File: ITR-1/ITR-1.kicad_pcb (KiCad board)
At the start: 2 copper layers, 30 x 40 mm, 4 parts, among them K1 кнопка

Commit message: схема организации питания
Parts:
- added C1: Конденсатор_керамический, N_RLC:Конденсатор_SMD_IEC_0805, F.Cu at (137.5, 47.5)
- added C2: Конденсатор_керамический, N_RLC:Конденсатор_SMD_IEC_0805, F.Cu at (137.5, 50.6)
- added C3: Конденсатор_керамический, N_RLC:Конденсатор_SMD_0603_pnp, F.Cu at (144.0, 47.4)
- added C4: Конденсатор_керамический, N_RLC:Конденсатор_SMD_IEC_0603, F.Cu at (141.8, 57.8)
- added C5: Конденсатор_керамический, N_RLC:Конденсатор_SMD_IEC_0603, F.Cu at (141.8, 60.5)
- added DD1: Микросхема_заряда_MCP73831T-2ACI_OT, N_G:SOT-23-5_pnp, F.Cu at (129.5, 31.8)
- added G2: ИОП_LM4040BIM3-2.5_NOPB, N_VD_HL:Транзистор_IRLML6344TR_SOT-23, F.Cu at (154.0, 40.0)
- added R1: Резистор_0,065Вт, N_RLC:Резистор_SMD_0603_0,065_Вт, F.Cu at (140.0, 35.7)
- added R10: Резистор_0,065Вт, N_RLC:Резистор_SMD_0603_0,065_Вт, F.Cu at (151.5, 64.2)
- added R11: Резистор_0,065Вт, N_RLC:Резистор_SMD_0603_0,065_Вт, F.Cu at (151.5, 67.3)
- added R12: Резистор_0,065Вт, N_RLC:Резистор_SMD_0603_0,065_Вт, F.Cu at (155.6, 64.2)
- added R2: Резистор_0,065Вт, N_RLC:Резистор_SMD_0603_0,065_Вт, F.Cu at (144.0, 35.7)
- added R3: Резистор_0,065Вт, N_RLC:Резистор_SMD_0603_0,065_Вт, F.Cu at (140.0, 38.8)
- added R4: Резистор_0,065Вт, N_RLC:Резистор_SMD_0603_0,065_Вт, F.Cu at (144.0, 38.8)
- added R5: Резистор_0,065Вт, N_RLC:Резистор_SMD_0603_0,065_Вт, F.Cu at (156.2, 49.2)
- added R6: Резистор_0,065Вт, N_RLC:Резистор_SMD_0603_0,065_Вт, F.Cu at (160.3, 49.2)
- added R7: Резистор_0,065Вт, N_RLC:Резистор_SMD_0603_0,065_Вт, F.Cu at (156.2, 52.3)
- added R8: Резистор_0,065Вт, N_RLC:Резистор_SMD_0603_0,065_Вт, F.Cu at (160.3, 52.3)
- added R9: Резистор_0,065Вт, N_RLC:Резистор_SMD_0603_0,065_Вт, F.Cu at (156.2, 55.4)
- added VD1: Диоды_шоттки_BAR43CFILM, N_VD_HL:Транзистор_IRLML6344TR_SOT-23, F.Cu at (152.0, 50.0)
- added VT1: Транзистор_полевой_P-канал(IRLML2246TRPBF), N_VD_HL:Транзистор_IRLML6344TR_SOT-23, F.Cu at (128.8, 38.2)
- added VT2: Транзистор_полевой_N-IRLML6344TR, N_VD_HL:Транзистор_IRLML6344TR_SOT-23, F.Cu at (135.8, 36.5)
- added VT3: Транзистор_полевой_N-IRLML6344TR, N_VD_HL:Транзистор_IRLML6344TR_SOT-23, F.Cu at (135.6, 41.0)
- added VT4: Транзистор_полевой_P-канал(IRLML2246TRPBF), N_VD_HL:Транзистор_IRLML6344TR_SOT-23, F.Cu at (152.0, 54.5)
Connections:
- G1 pad 1: (no net) -> /GND
- G1 pad 2: (no net) -> /3V3
- G1 pad 3: (no net) -> /BAT.LOAD
- G1 pad 4: (no net) -> /3V3

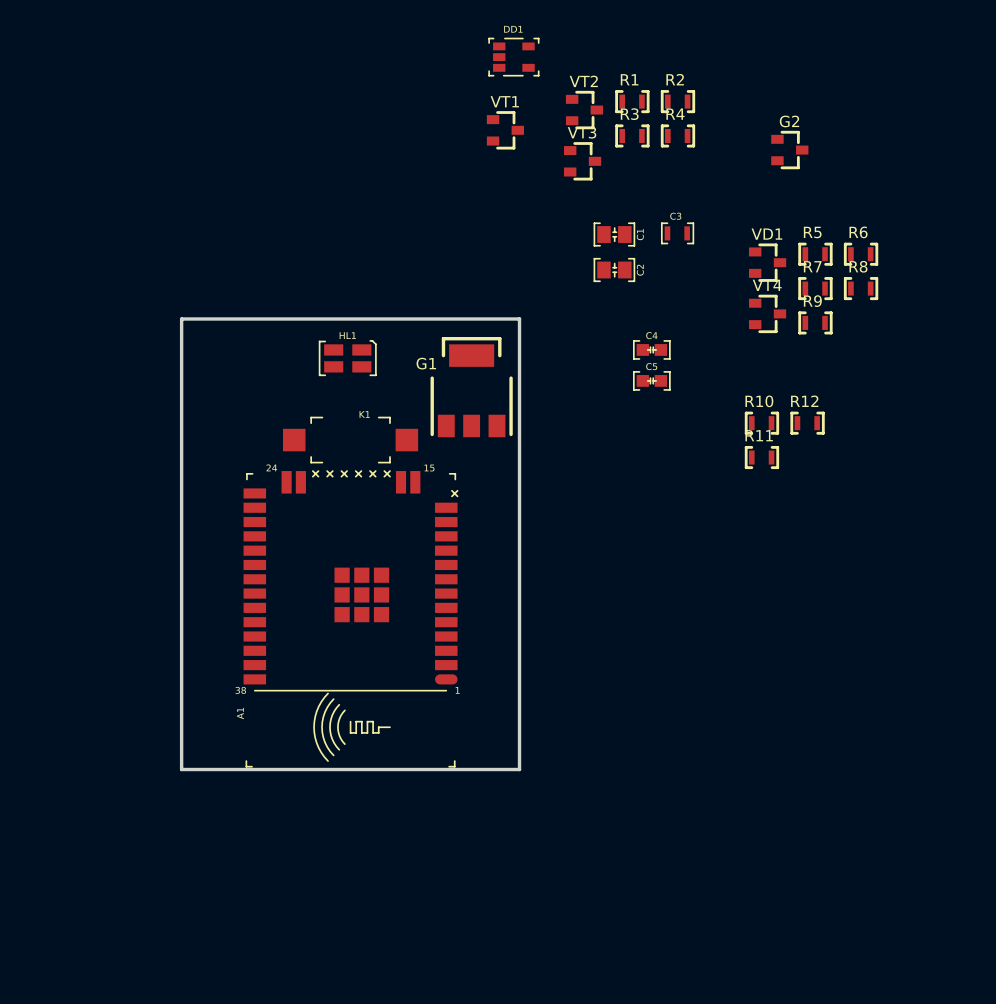
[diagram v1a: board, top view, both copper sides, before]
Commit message: закончена схема, начата трассировка питания
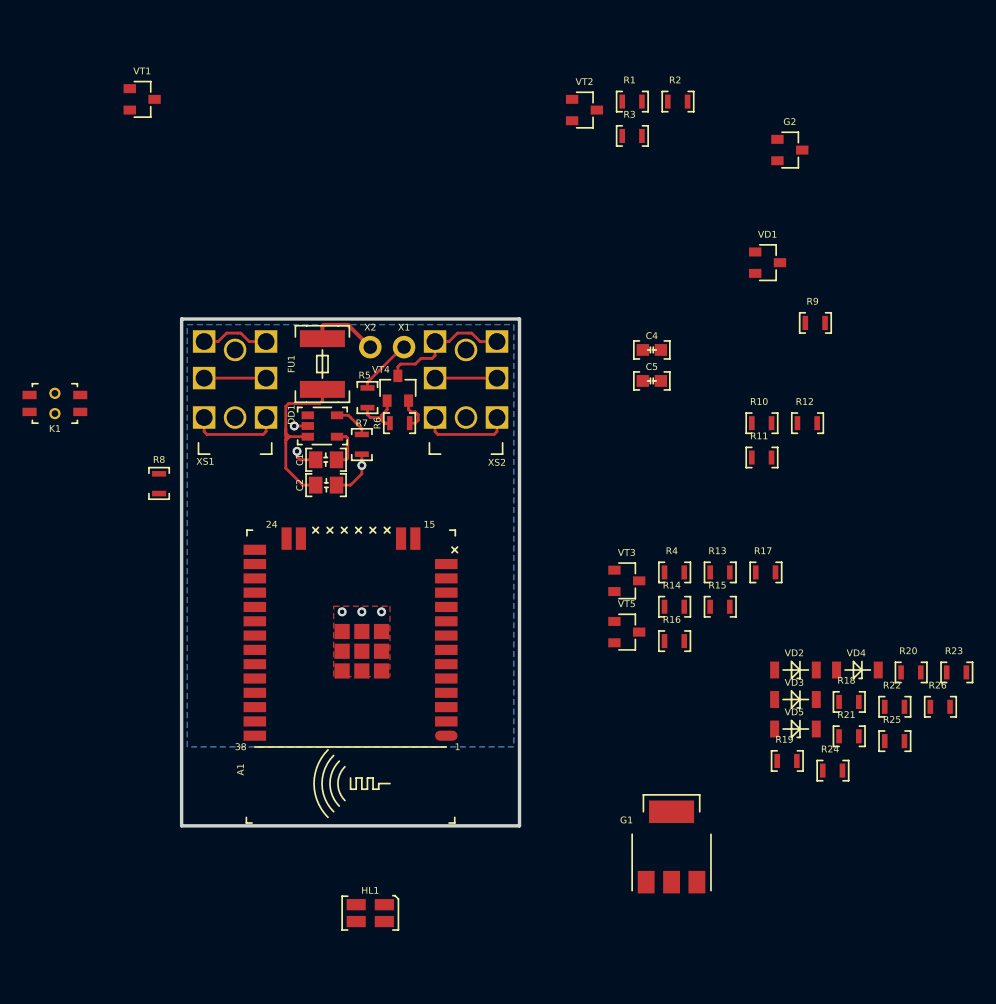
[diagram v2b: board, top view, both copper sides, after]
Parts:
- removed C3: Конденсатор_керамический, N_RLC:Конденсатор_SMD_0603_pnp
- added FU1: Предохранитель_MF-MSMF030, N_RLC:Предохранитель_SMD_1812, F.Cu at (112.5, 56.8)
- added R13: Резистор_0,065Вт, N_RLC:Резистор_SMD_0603_0,065_Вт, F.Cu at (147.8, 77.5)
- added R14: Резистор_0,065Вт, N_RLC:Резистор_SMD_0603_0,065_Вт, F.Cu at (143.8, 80.5)
- added R15: Резистор_0,065Вт, N_RLC:Резистор_SMD_0603_0,065_Вт, F.Cu at (147.8, 80.5)
- added R16: Резистор_0,065Вт, N_RLC:Резистор_SMD_0603_0,065_Вт, F.Cu at (143.8, 83.6)
- added R17: Резистор_0,065Вт, N_RLC:Резистор_SMD_0603_0,065_Вт, F.Cu at (151.8, 77.5)
- added R18: Резистор_0,065Вт, N_RLC:Резистор_SMD_0603_0,065_Вт, F.Cu at (159.2, 89.0)
- added R19: Резистор_0,065Вт, N_RLC:Резистор_SMD_0603_0,065_Вт, F.Cu at (153.8, 94.2)
- added R20: Резистор_0,065Вт, N_RLC:Резистор_SMD_0603_0,065_Вт, F.Cu at (164.8, 86.4)
- added R21: Резистор_0,065Вт, N_RLC:Резистор_SMD_0603_0,065_Вт, F.Cu at (159.2, 92.0)
- added R22: Резистор_0,065Вт, N_RLC:Резистор_SMD_0603_0,065_Вт, F.Cu at (163.3, 89.4)
- added R23: Резистор_0,065Вт, N_RLC:Резистор_SMD_0603_0,065_Вт, F.Cu at (168.8, 86.4)
- added R24: Резистор_0,065Вт, N_RLC:Резистор_SMD_0603_0,065_Вт, F.Cu at (157.8, 95.1)
- added R25: Резистор_0,065Вт, N_RLC:Резистор_SMD_0603_0,065_Вт, F.Cu at (163.3, 92.5)
- added R26: Резистор_0,065Вт, N_RLC:Резистор_SMD_0603_0,065_Вт, F.Cu at (167.3, 89.4)
- added VD2: Стабилитрон_BZV55C2V7, N_VD_HL:SOD-80, F.Cu at (152.6, 86.2)
- added VD3: Стабилитрон_BZV55C2V7, N_VD_HL:SOD-80, F.Cu at (152.6, 88.8)
- added VD4: Стабилитрон_BZV55C2V7, N_VD_HL:SOD-80, F.Cu at (158.1, 86.2)
- added VD5: Стабилитрон_BZV55-C3V9, N_VD_HL:SOD-80, F.Cu at (152.6, 91.4)
- added VT5: Транзистор_полевой_N-IRLML6344TR, N_VD_HL:Транзистор_IRLML6344TR_SOT-23, F.Cu at (139.5, 82.8)
- added X1: отверстие_под_пайку, N_X:ОтверстиеD1.2, F.Cu at (119.8, 57.5)
- added X2: отверстие_под_пайку, N_X:ОтверстиеD1.2, F.Cu at (116.8, 57.5)
- added XS1: Клеммник_х3, N_X:jack_ST-033, F.Cu at (102.2, 63.8)
- added XS2: Клеммник_х3, N_X:jack_ST-033, F.Cu at (122.8, 63.8)
- K1: value кнопка -> Кнопка_KLS7-TS5401-1.35-250-T; footprint N_X:Кнопка_FSMSM -> N_X:Кнопка_KLS7-TS5401
- moved R8 64.7 mm to (98.0, 69.6), turned to 90 degrees
- moved HL1 49.3 mm to (118.0, 107.0)
- moved G1 44.2 mm to (143.5, 101.2)
- moved R6 43.6 mm to (119.4, 64.2), turned to 180 degrees
- moved R7 42.6 mm to (116.0, 66.1), turned to 270 degrees
- moved R5 41.7 mm to (116.5, 62.0), turned to 90 degrees
- moved R4 38.8 mm to (143.8, 77.5)
- moved VT3 37.5 mm to (139.5, 78.2)
- moved DD1 36.9 mm to (112.5, 64.5)
- moved VT4 33.5 mm to (119.2, 61.1), turned to 90 degrees
- moved VT1 32.4 mm to (96.5, 35.5)
- moved C2 31.9 mm to (111.9, 69.8)
- moved C1 31.0 mm to (113.8, 67.5), turned to 180 degrees
- moved K1 19.4 mm to (91.0, 61.8), turned to 180 degrees
- moved A1 5.00 mm to (115.0, 83.0)
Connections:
- net /BAT.IN renamed Net-(C2-Pad1)
- net Net-(R9-Pad2) renamed /EXT.BUTT
- A1 pad 1: (no net) -> /GND
- A1 pad 11: (no net) -> /BUTT.TURN
- A1 pad 13: (no net) -> /CHARGE.MODE
- A1 pad 15: (no net) -> /GND
- A1 pad 2: (no net) -> /3V3
- A1 pad 25: (no net) -> /BOOT
- A1 pad 29: (no net) -> /LED.RED
- A1 pad 3: (no net) -> /RESET
- A1 pad 31: (no net) -> /LED.GREEN
- A1 pad 34: (no net) -> /UART.RX
- A1 pad 35: (no net) -> /UART.TX
- A1 pad 38: (no net) -> /GND
- A1 pad 39: Net-(A1-Pad39) -> /GND
- A1 pad 6: (no net) -> /2V5.REF
- A1 pad 7: (no net) -> /BAT.MEASURE
- A1 pad 9: (no net) -> /SELF.TURN
- HL1 pad 1: (no net) -> /3V3
- HL1 pad 2: (no net) -> Net-(HL1-Pad2)
- HL1 pad 3: (no net) -> /3V3
- HL1 pad 4: (no net) -> Net-(HL1-Pad4)
- K1 pad 1: (no net) -> Net-(K1-Pad1)
- K1 pad 2: (no net) -> Net-(K1-Pad1)
- R3 pad 1: (no net) -> /SELF.TURN
- R4 pad 1: (no net) -> Net-(R14-Pad2)
- R4 pad 2: (no net) -> /LED.GREEN
- R8 pad 1: (no net) -> /CHARGE.MODE
- R9 pad 1: (no net) -> /BUTT.TURN
- VT3 pad 1: (no net) -> Net-(R14-Pad2)
- VT3 pad 2: (no net) -> /GND
- VT3 pad 3: (no net) -> Net-(R16-Pad2)
- VT4 pad 3: (no net) -> /U.IN
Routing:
- net /GND: track 0.00 -> 21.1 mm, vias 0 -> 6
- net Net-(C2-Pad1): track 0.00 -> 16.7 mm
- net /U.IN: track 0.00 -> 11.9 mm
- net /OUT.BOOT: track 0.00 -> 8.21 mm
- net /U.PROTECT: track 0.00 -> 7.01 mm
- net /BAT.IN: track 0.00 -> 6.22 mm
- net /OUT.RX: track 0.00 -> 6.12 mm
- net /OUT.TX: track 0.00 -> 5.50 mm
- net /EXT.BUTT: track 0.00 -> 5.50 mm
- net Net-(R5-Pad1): track 0.00 -> 5.04 mm
- net Net-(DD1-Pad5): track 0.00 -> 3.20 mm
- added copper zone on B.Cu, net /GND
- added copper zone on F.Cu, net /GND
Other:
- board size 30 x 40 mm -> 30 x 45 mm
- net class BATT added: clearance 0.2, trace_width 0.35, via_dia 1, via_drill 0.6

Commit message: подготовлена трассировка питания, упрощена схема подключения периферии
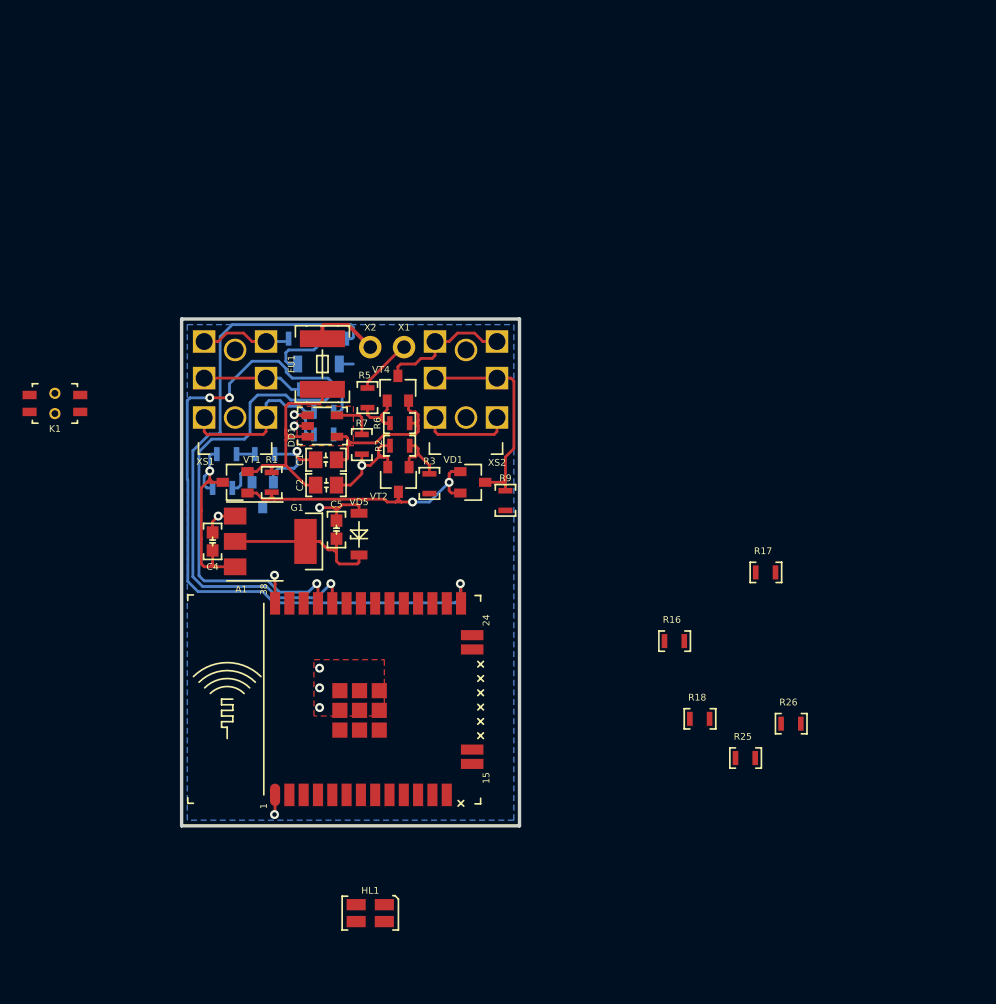
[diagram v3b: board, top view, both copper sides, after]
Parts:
- removed R13, R14, R15, R23, R24, R4: Резистор_0,065Вт, N_RLC:Резистор_SMD_0603_0,065_Вт
- removed VD2, VD3: Стабилитрон_BZV55C2V7, N_VD_HL:SOD-80
- removed VT3, VT5: Транзистор_полевой_N-IRLML6344TR, N_VD_HL:Транзистор_IRLML6344TR_SOT-23
- G2, R10, R11, R12, R19, R20, R21, R22, R8, VD4: moved to B.Cu
- moved R22 59.4 mm to (113.8, 56.8), turned to 180 degrees
- moved R20 59.0 mm to (111.4, 61.2), turned to 180 degrees
- moved R19 57.3 mm to (110.4, 56.8), turned to 180 degrees
- moved G2 55.9 mm to (107.2, 70.6), turned to 270 degrees
- moved R21 54.8 mm to (112.6, 63.2), turned to 180 degrees
- moved R12 52.2 mm to (103.6, 70.0)
- moved VD4 51.8 mm to (114.0, 59.0), turned to 180 degrees
- moved R10 47.6 mm to (104.0, 67.0)
- moved R1 46.5 mm to (108.0, 69.5), turned to 270 degrees
- moved R11 44.1 mm to (107.4, 67.0)
- moved G1 43.9 mm to (108.5, 74.8), turned to 270 degrees
- moved C4 42.5 mm to (102.8, 74.8), turned to 90 degrees
- moved VD5 41.6 mm to (115.8, 72.2), turned to 270 degrees
- moved R2 39.3 mm to (119.4, 66.2), turned to 180 degrees
- moved VT2 36.7 mm to (119.2, 69.2), turned to 270 degrees
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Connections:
- net Net-(C2-Pad1) renamed /BAT.CHARGE
- A1 pad 29: /LED.RED -> /LED.GREEN
- A1 pad 31: /LED.GREEN -> /LED.RED
- HL1 pad 1: /3V3 -> Net-(HL1-Pad1)
- HL1 pad 2: Net-(HL1-Pad2) -> /GND
- HL1 pad 3: /3V3 -> Net-(HL1-Pad3)
- HL1 pad 4: Net-(HL1-Pad4) -> /GND
- R16 pad 1: Net-(HL1-Pad4) -> Net-(HL1-Pad1)
- R16 pad 2: Net-(R16-Pad2) -> /LED.RED
- R17 pad 1: Net-(HL1-Pad2) -> Net-(HL1-Pad3)
- R17 pad 2: Net-(R17-Pad2) -> /LED.GREEN
- R18 pad 1: Net-(R18-Pad1) -> /BOOT
- R20 pad 1: Net-(R20-Pad1) -> /UART.TX
- R21 pad 1: Net-(R18-Pad1) -> /BOOT
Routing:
- net /BOOT: track 0.00 -> 63.6 mm, vias 0 -> 3
- net /UART.RX: track 0.00 -> 52.1 mm, vias 0 -> 1
- net /UART.TX: track 0.00 -> 40.9 mm, vias 0 -> 1
- net /GND: track 21.1 -> 48.6 mm, vias 6 -> 10
- net Net-(R1-Pad2): track 0.00 -> 25.0 mm, vias 0 -> 2
- net /BAT.LOAD: track 0.00 -> 19.7 mm, vias 0 -> 1
- net /3V3: track 0.00 -> 14.6 mm
- net /EXT.BUTT: track 5.50 -> 19.4 mm
- net /U.PROTECT: track 7.01 -> 15.7 mm
- net Net-(R19-Pad1): track 0.00 -> 7.69 mm
- net /OUT.BOOT: track 8.21 -> 14.2 mm
- net Net-(R2-Pad1): track 0.00 -> 5.26 mm
- net /BAT.CHARGE: track 16.7 -> 21.2 mm
- net Net-(DD1-Pad1): track 0.00 -> 4.32 mm, vias 0 -> 1
- net /2V5.REF: track 0.00 -> 3.84 mm
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- added copper zone on F.Cu, net /BAT.CHARGE

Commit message: обновлены посадочные места и схема питания
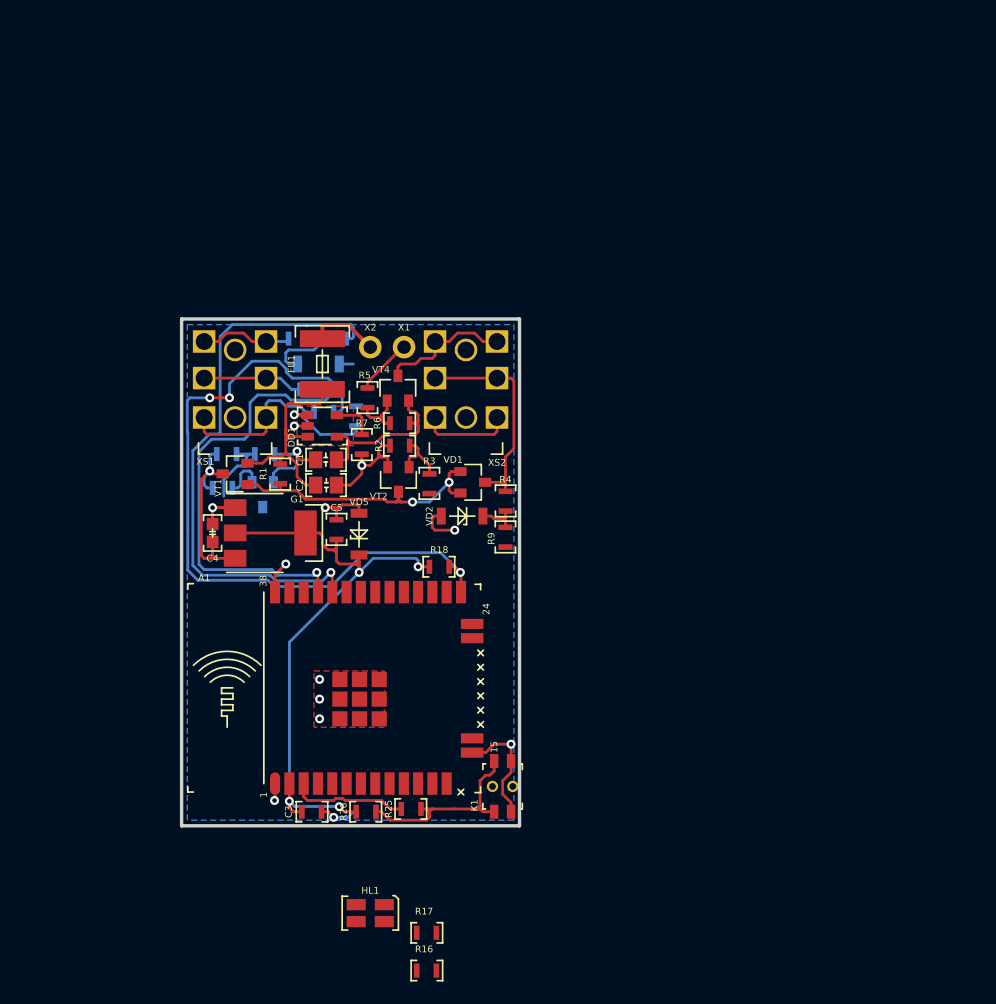
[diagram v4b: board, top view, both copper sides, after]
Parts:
- added C3: Конденсатор_керамический, N_RLC:Конденсатор_SMD_0603_pnp, F.Cu at (111.5, 98.8)
- added R4: Резистор_0,065Вт, N_RLC:Резистор_SMD_0603_0,065_Вт, F.Cu at (128.8, 71.2)
- added VD2: Стабилитрон_BZV55-C3V9, N_VD_HL:SOD-80, F.Cu at (123.0, 72.5)
- C5: footprint N_RLC:Конденсатор_SMD_IEC_0603 -> N_RLC:Конденсатор_SMD_0603_pnp
- moved K1 53.2 mm to (129.2, 98.8), turned to 90 degrees
- moved R17 43.9 mm to (121.8, 109.5)
- moved R26 38.5 mm to (116.4, 98.8), turned to 180 degrees
- moved R16 36.6 mm to (121.8, 112.8)
- moved R25 30.0 mm to (120.4, 98.5), turned to 180 degrees
- moved R18 26.8 mm to (122.9, 77.0), turned to 180 degrees
- moved R8 3.30 mm to (115.5, 63.6), turned to 270 degrees
- moved R9 3.25 mm to (128.8, 74.4)
- moved R1 1.06 mm to (108.8, 68.8)
- moved A1 1.00 mm to (117.3, 87.8)
- moved C4 0.75 mm to (102.8, 74.0)
- moved G1 0.75 mm to (108.5, 74.0)
- moved VT1 0.75 mm to (104.8, 68.8)
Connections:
- net /BAT.MEASURE renamed /AN.BAT.MEASURE
- A1 pad 5: (no net) -> /AN.2V5.REF
- A1 pad 6: /2V5.REF -> (no net)
- G2 pad 1: /2V5.REF -> /AN.2V5.REF
- R12 pad 2: /2V5.REF -> /AN.2V5.REF
- R9 pad 2: /EXT.BUTT -> Net-(R4-Pad1)
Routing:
- net /3V3: track 14.6 -> 57.4 mm, vias 0 -> 4
- net /GND: track 48.6 -> 68.8 mm, vias 10 -> 13
- net Net-(K1-Pad1): track 0.00 -> 18.6 mm
- net /RESET: track 0.00 -> 10.4 mm
- net /AN.BAT.MEASURE: track 1.62 -> 7.35 mm
- net Net-(R4-Pad1): track 0.00 -> 4.06 mm
- net /AN.2V5.REF: track 0.00 -> 3.84 mm
- net /2V5.REF: track 3.84 -> 0.00 mm
- net Net-(DD1-Pad1): track 4.32 -> 8.05 mm
- net /UART.TX: track 40.9 -> 39.5 mm
- net /UART.RX: track 52.1 -> 50.6 mm
- net /BAT.LOAD: track 19.7 -> 18.4 mm
- net Net-(R1-Pad2): track 25.0 -> 25.8 mm
- net /BOOT: track 63.6 -> 64.2 mm

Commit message: подготовлена трассировка +PNG +STP, требуется контрольная проверка
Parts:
- removed R16: Резистор_0,065Вт, N_RLC:Резистор_SMD_0603_0,065_Вт
- added D1: LOGO, N_ICO:ni_10x10, B.Cu at (105.0, 89.0)
- added D2: LOGO, N_ICO:VLAD_10x10, B.Cu at (116.0, 88.8)
- HL1: value Светодиод_сдвоенный_KPB-3025SURKCGKC -> Светодиод; footprint N_VD_HL:Светодиод_SMD_m3025 -> N_VD_HL:Светодиод_SMD_IEC_0603
- moved R17 35.0 mm to (120.5, 74.5), turned to 270 degrees
- moved HL1 32.3 mm to (118.5, 74.8), turned to 90 degrees
- moved R18 3.88 mm to (126.8, 77.0), turned to 0 degrees
- moved R9 2.00 mm to (126.8, 74.5), turned to 0 degrees
- moved C4 0.67 mm to (103.2, 74.5)
- moved C5 0.50 mm to (114.2, 73.7)
- moved G1 0.50 mm to (109.0, 74.0)
- moved VD5 0.50 mm to (116.2, 72.2)
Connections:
- A1 pad 11: /BUTT.TURN -> (no net)
- A1 pad 13: /CHARGE.MODE -> (no net)
- A1 pad 24: (no net) -> /AN.2V5.REF
- A1 pad 26: (no net) -> /AN.BAT.MEASURE
- A1 pad 28: (no net) -> /BUTT.TURN
- A1 pad 29: /LED.GREEN -> /SELF.TURN
- A1 pad 30: (no net) -> /LED
- A1 pad 31: /LED.RED -> /CHARGE.MODE
- A1 pad 5: /AN.2V5.REF -> (no net)
- A1 pad 7: /AN.BAT.MEASURE -> (no net)
- A1 pad 9: /SELF.TURN -> (no net)
- R17 pad 1: Net-(HL1-Pad3) -> Net-(HL1-PadA)
- R17 pad 2: /LED.GREEN -> /LED
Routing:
- net /AN.2V5.REF: track 3.84 -> 47.2 mm, vias 0 -> 1
- net /GND: track 68.8 -> 101.4 mm, vias 13 -> 14
- net /AN.BAT.MEASURE: track 7.35 -> 38.4 mm, vias 0 -> 1
- net /CHARGE.MODE: track 0.00 -> 19.6 mm, vias 0 -> 1
- net /SELF.TURN: track 0.00 -> 10.0 mm
- net /BUTT.TURN: track 0.00 -> 7.72 mm
- net Net-(HL1-PadA): track 0.00 -> 6.62 mm
- net /3V3: track 57.4 -> 64.0 mm
- net /LED: track 0.00 -> 5.05 mm
- net Net-(R4-Pad1): track 4.06 -> 5.89 mm
- net /BAT.LOAD: track 18.4 -> 19.0 mm
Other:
- board text added: "BAT+"
- board text added: "BAT-"
- board text added: "BOOT"
- board text added: "BUTT"
- board text added: "GND"
- board text added: "ITR-1-0N9"
- board text added: "RESET"
- board text added: "RX"
- board text added: "TX"
- board text added: "UIN"
- board text added: "ЗОНА УСТАНОВКИ АККУМУЛЯТОРА"
